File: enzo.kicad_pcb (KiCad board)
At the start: 2 copper layers, 118 x 95.1 mm, 59 parts, among them SW1 SW_Push, SW10 SW_Push, SW11 SW_Push, SW12 SW_Push, SW13 SW_Push, SW14 SW_Push, SW15 SW_Push, SW16 SW_Push, SW17 locked, SW2 SW_Push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

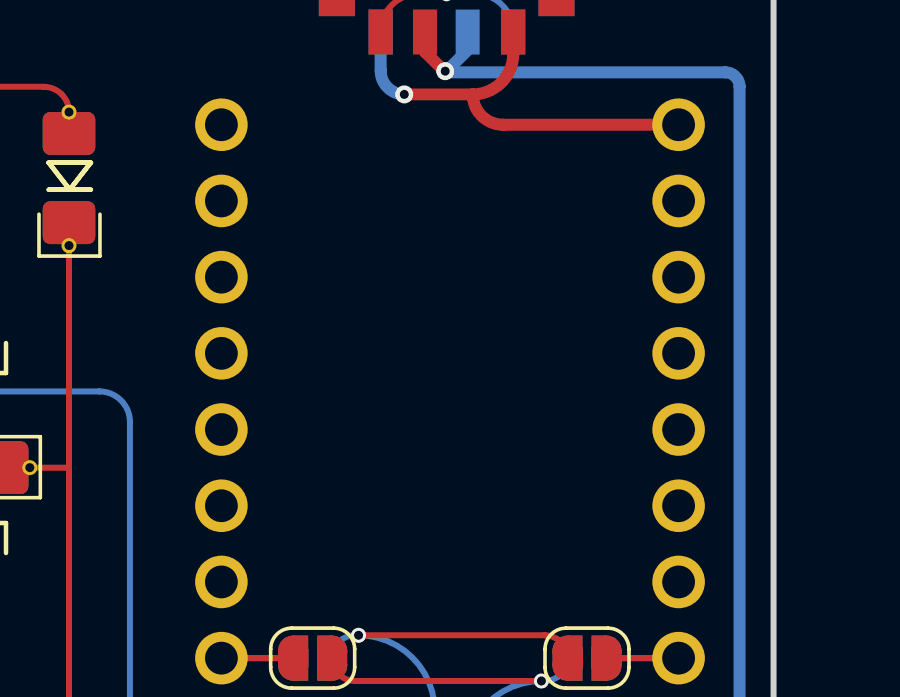
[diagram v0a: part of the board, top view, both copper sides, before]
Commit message: Add reset button footprint
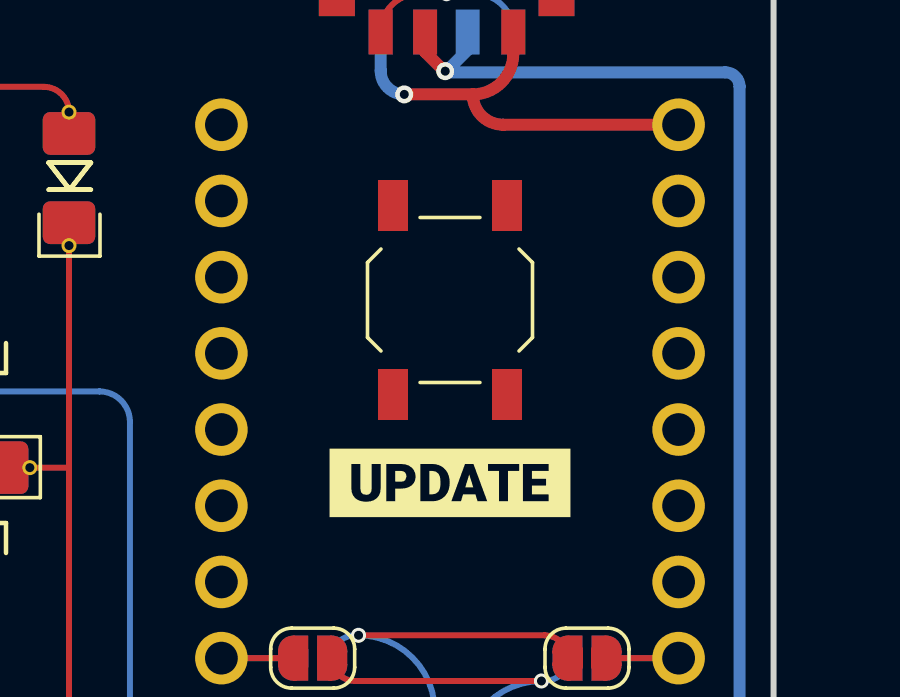
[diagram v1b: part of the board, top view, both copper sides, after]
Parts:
- added REF**: SW_SPST_TL3342, Button_Switch_SMD:SW_SPST_TL3342, B.Cu at (188.0, 72.1)
- added REF**: SW_SPST_TL3342, Button_Switch_SMD:SW_SPST_TL3342, F.Cu at (188.0, 72.1)
- added kibuzzard-61F01C84: G***, local-libraries:kibuzzard-61F01C84, F.Cu at (188.0, 78.2)
- added kibuzzard-61F01C84: G***, local-libraries:kibuzzard-61F01C84, B.Cu at (188.0, 78.2)

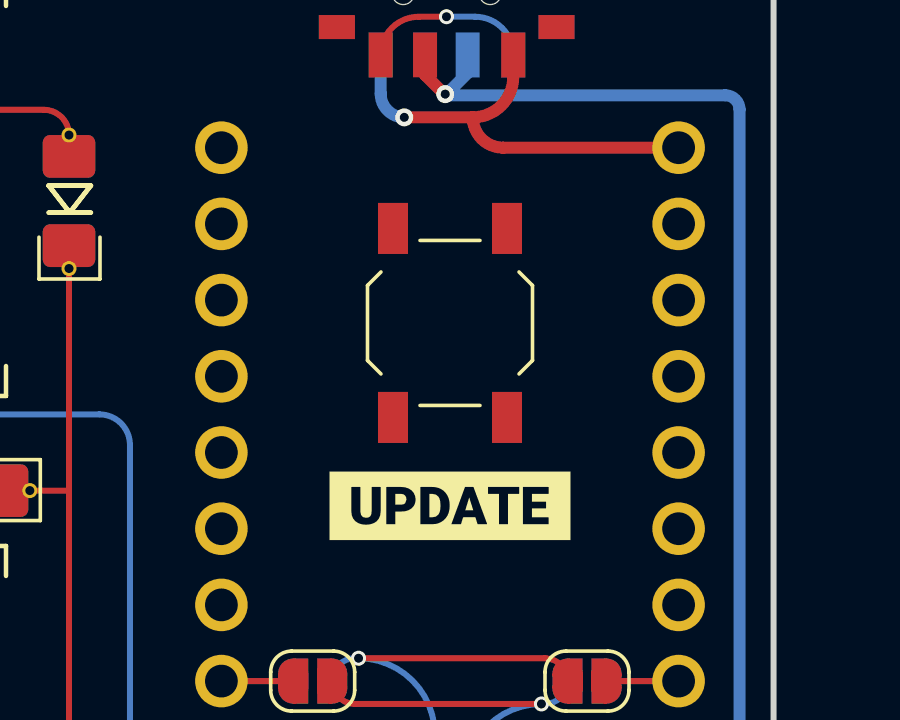
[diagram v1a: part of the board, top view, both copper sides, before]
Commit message: Add traces for the reset button
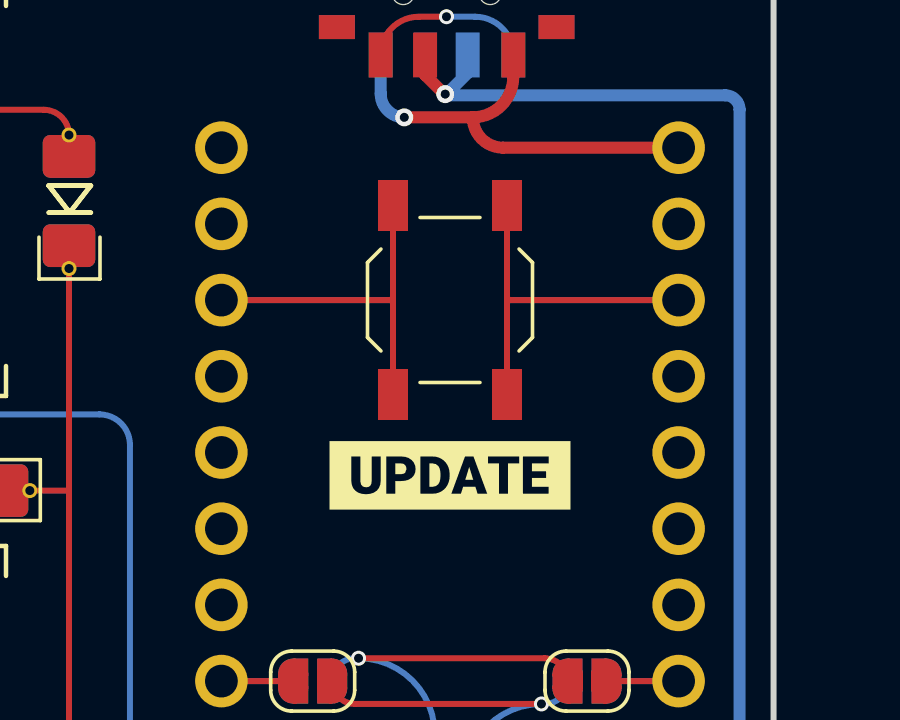
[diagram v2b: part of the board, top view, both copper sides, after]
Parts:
- moved kibuzzard-61F01C84 1.02 mm to (188.0, 77.2) (x2)
- moved REF** 0.77 mm to (188.0, 71.4) (x2)
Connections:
- REF** pad 1: (no net) -> rst
- REF** pad 2: (no net) -> grnd
- REF** pad 1: (no net) -> grnd
- REF** pad 2: (no net) -> rst
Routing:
- net rst: track 0.00 -> 24.2 mm
- net grnd: track 0.00 -> 24.2 mm

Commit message: Minor trace tweaks/cleanup
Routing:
- net grnd: track 24.2 -> 30.3 mm
- net rst: track 24.2 -> 30.3 mm
- net row2_matrix: track 226.8 -> 232.4 mm
- net col2_matrix: track 148.0 -> 147.0 mm
- net col1_matrix: track 166.6 -> 166.1 mm
- net row3_matrix: track 211.6 -> 212.1 mm

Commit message: Use the proper ground layer
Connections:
- REF** pad 2: grnd -> Gnd_l (x2)
- REF** pad 23: grnd -> Gnd_l
- REF** pad 3: grnd -> Gnd_l
- REF** pad 4: grnd -> Gnd_l
- REF** pad 1: grnd -> Gnd_l
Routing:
- net grnd: track 30.3 -> 0.00 mm
- net Gnd_l: track 0.00 -> 30.3 mm

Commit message: Fix design
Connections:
- REF** pad 1: (no net) -> Net-(Row5-unused) (x3)
- REF** pad 2: (no net) -> Net-(Row5-unused)
- REF** pad 12: (no net) -> Net-(Row5-unused)
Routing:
- net Net-(Row5-unused): track 0.00 -> 13.4 mm, vias 0 -> 1
- net (no net): track 8.54 -> 0.00 mm, vias 1 -> 0
- net col5_matrix: track 91.5 -> 86.7 mm
- net batt_conn: track 52.0 -> 50.9 mm
- net Net-(D15-Pad2): track 24.7 -> 23.7 mm
- net unconnected-(PSW1-Pad3): track 6.55 -> 5.77 mm
- net Net-(D10-Pad2): track 24.5 -> 23.9 mm
- net Net-(D5-Pad2): track 24.1 -> 23.5 mm
- net Net-(D14-Pad2): track 24.0 -> 23.5 mm
- net row2_matrix: track 232.4 -> 232.9 mm
- net row3_matrix: track 212.1 -> 211.6 mm

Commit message: PCB: fix mcu pins definition
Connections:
- REF** pad 2: col4_matrix -> col4_mcu
- REF** pad 1: row2_matrix -> row2_mcu
- REF** pad 2: col1_matrix -> col1_mcu
- REF** pad 2: col3_matrix -> col3_mcu
- REF** pad 1: col1_matrix -> col1_mcu
- REF** pad 1: col5_matrix -> col5_mcu
- REF** pad 2: row3_matrix -> row3_mcu
- REF** pad 2: row1_matrix -> row1_mcu
- REF** pad 1: col2_matrix -> col2_mcu
- REF** pad 2: row2_matrix -> row2_mcu
- REF** pad 1: col4_matrix -> col4_mcu
- REF** pad 1: col3_matrix -> col3_mcu
- REF** pad 2: row4_matrix -> row4_mcu
- REF** pad 2: col5_matrix -> col5_mcu
- REF** pad 10: row3_matrix -> row3_mcu
- REF** pad 11: row4_matrix -> row4_mcu
- REF** pad 13: col5_matrix -> col5_mcu
- REF** pad 14: col4_matrix -> col4_mcu
- REF** pad 15: col3_matrix -> col3_mcu
- REF** pad 16: col2_matrix -> col2_mcu
- REF** pad 17: col1_matrix -> col1_mcu
- REF** pad 8: row1_matrix -> row1_mcu
- REF** pad 9: row2_matrix -> row2_mcu
- REF** pad 1: row4_matrix -> row4_mcu
- REF** pad 2: col2_matrix -> col2_mcu
- REF** pad 1: row3_matrix -> row3_mcu
- REF** pad 1: row1_matrix -> row1_mcu
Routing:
- net col1_mcu: track 0.00 -> 4.81 mm
- net col1_matrix: track 166.5 -> 161.7 mm
- net col2_mcu: track 0.00 -> 4.80 mm
- net col2_matrix: track 147.2 -> 142.4 mm
- net col3_mcu: track 0.00 -> 4.80 mm
- net col3_matrix: track 118.9 -> 114.1 mm
- net col4_mcu: track 0.00 -> 4.80 mm
- net col4_matrix: track 123.0 -> 118.2 mm
- net row4_mcu: track 0.00 -> 4.80 mm
- net row4_matrix: track 228.9 -> 224.1 mm
- net col5_mcu: track 0.00 -> 4.80 mm
- net col5_matrix: track 86.7 -> 81.9 mm
- net row3_mcu: track 0.00 -> 4.79 mm
- net row3_matrix: track 211.6 -> 206.8 mm
- net row2_mcu: track 0.00 -> 4.79 mm
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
